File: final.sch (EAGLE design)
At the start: 84 parts, among them IC2 MEGA8-AI, IC4 7805, Q2 32.768kHz, U2 DS1307

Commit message: added holes and milling
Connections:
- removed net N$11: IC2.PB5(SCK), JP16.9
- removed net N$12: IC2.PB4(MISO), JP16.8
- removed net N$13: IC2.PB3(MOSI/OC2), JP16.7
- new net SELECT4.1: JP4.4, R36.2
- net MISO: now also IC2.PB4(MISO), JP16.8
- net MOSI: now also IC2.PB3(MOSI/OC2), JP16.7
- net SCK: now also IC2.PB5(SCK), JP16.9; no longer JP4.4, R36.2
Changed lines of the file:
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@@
 <net name="SCK" class="0">
-<segment>
-<pinref part="R36" gate="G$1" pin="2"/>
-<label x="464.82" y="5.08" size="1.778" layer="95"/>
-<pinref part="JP4" gate="A" pin="4"/>
-<wire x1="568.96" y1="137.16" x2="480.06" y2="137.16" width="0.1524" layer="91"/>
-<wire x1="480.06" y1="137.16" x2="480.06" y2="5.08" width="0.1524" layer="91"/>
-<wire x1="480.06" y1="5.08" x2="459.74" y2="5.08" width="0.1524" layer="91"/>
-<label x="546.1" y="137.16" size="1.778" layer="95"/>
-</segment>
 <segment>
 <pinref part="JP13" gate="A" pin="3"/>
 <wire x1="259.08" y1="-259.08" x2="248.92" y2="-259.08" width="0.1524" layer="91"/>
 <label x="248.92" y="-259.08" size="1.778" layer="95"/>
+</segment>
+<segment>
+<pinref part="IC2" gate="G$1" pin="PB5(SCK)"/>
+<label x="292.1" y="-223.52" size="1.778" layer="95"/>
+<pinref part="JP16" gate="A" pin="9"/>
+<wire x1="292.1" y1="-223.52" x2="330.2" y2="-223.52" width="0.1524" layer="91"/>
 </segment>
 </net>
@@
 <label x="248.92" y="-256.54" size="1.778" layer="95"/>
 </segment>
+<segment>
+<pinref part="IC2" gate="G$1" pin="PB4(MISO)"/>
+<wire x1="299.72" y1="-220.98" x2="297.18" y2="-220.98" width="0.1524" layer="91"/>
+<label x="292.1" y="-220.98" size="1.778" layer="95"/>
+<pinref part="JP16" gate="A" pin="8"/>
+<wire x1="297.18" y1="-220.98" x2="292.1" y2="-220.98" width="0.1524" layer="91"/>
+<wire x1="330.2" y1="-220.98" x2="299.72" y2="-220.98" width="0.1524" layer="91"/>
+</segment>
 </net>
 <net name="MOSI" class="0">
@@
 <wire x1="266.7" y1="-259.08" x2="276.86" y2="-259.08" width="0.1524" layer="91"/>
 <label x="271.78" y="-259.08" size="1.778" layer="95"/>
+</segment>
+<segment>
+<pinref part="IC2" gate="G$1" pin="PB3(MOSI/OC2)"/>
+<label x="292.1" y="-218.44" size="1.778" layer="95"/>
+<pinref part="JP16" gate="A" pin="7"/>
+<wire x1="330.2" y1="-218.44" x2="292.1" y2="-218.44" width="0.1524" layer="91"/>
 </segment>
 </net>
@@
 </segment>
 </net>
-<net name="N$11" class="0">
-<segment>
-<pinref part="IC2" gate="G$1" pin="PB5(SCK)"/>
-<label x="292.1" y="-223.52" size="1.778" layer="95"/>
-<pinref part="JP16" gate="A" pin="9"/>
-<wire x1="292.1" y1="-223.52" x2="330.2" y2="-223.52" width="0.1524" layer="91"/>
-</segment>
-</net>
-<net name="N$12" class="0">
-<segment>
-<pinref part="IC2" gate="G$1" pin="PB4(MISO)"/>
-<wire x1="299.72" y1="-220.98" x2="297.18" y2="-220.98" width="0.1524" layer="91"/>
-<label x="292.1" y="-220.98" size="1.778" layer="95"/>
-<pinref part="JP16" gate="A" pin="8"/>
-<wire x1="297.18" y1="-220.98" x2="292.1" y2="-220.98" width="0.1524" layer="91"/>
-<wire x1="330.2" y1="-220.98" x2="299.72" y2="-220.98" width="0.1524" layer="91"/>
-</segment>
-</net>
-<net name="N$13" class="0">
-<segment>
-<pinref part="IC2" gate="G$1" pin="PB3(MOSI/OC2)"/>
-<label x="292.1" y="-218.44" size="1.778" layer="95"/>
-<pinref part="JP16" gate="A" pin="7"/>
-<wire x1="330.2" y1="-218.44" x2="292.1" y2="-218.44" width="0.1524" layer="91"/>
-</segment>
-</net>
 <net name="N$15" class="0">
 <segment>
@@
 </segment>
 </net>
+<net name="SELECT4.1" class="0">
+<segment>
+<pinref part="R36" gate="G$1" pin="2"/>
+<label x="464.82" y="5.08" size="1.778" layer="95"/>
+<pinref part="JP4" gate="A" pin="4"/>
+<wire x1="568.96" y1="137.16" x2="480.06" y2="137.16" width="0.1524" layer="91"/>
+<wire x1="480.06" y1="137.16" x2="480.06" y2="5.08" width="0.1524" layer="91"/>
+<wire x1="480.06" y1="5.08" x2="459.74" y2="5.08" width="0.1524" layer="91"/>
+<label x="546.1" y="137.16" size="1.778" layer="95"/>
+</segment>
+</net>

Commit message: moved 1k resisitors on logic board, more compact. fixed inductor, diode and 7805 packages. TODO add ground plane, move holes, add milling
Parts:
- removed IC4: 7805, v-reg:LD117ADT18TR
- removed R10, R12, R14, R16, R18, R20, R73, R8, R9: 1k, eagle-ltspice:RR1206
- added IC1: LD117ADT12TR, v-reg:LD117ADT12TR
- added R24, R25, R26, R28, R30, R32, R33, R34, R35: 1k, eagle-ltspice:RR1206
- C13: value (none) -> 120pF
- C14, C15: value (none) -> 22uF
- C16: value 10uF -> 22uF
- C18: value 22uF -> 10uF
- R69: value (none) -> 13k
- R70: value (none) -> 200k
- R71, R72: value 1k -> 10k
- U$7: value INDUCTOR -> 15uH
- renumbered U$16 to U$6, U$17 to U$7, U$19 to U$8, U$20 to U$5
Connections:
- removed net N$1: JP3.1, R73.2
- new net N$48: JP16.1, R24.1
- net +5V: now also IC1.OUT; no longer IC4.OUT
- net GND: now also IC1.ADJ; no longer IC4.ADJ
- net MISO: now also R34.2; no longer JP16.8
- net MOSI: now also R32.2; no longer JP16.7
- net N$15: now also R33.2; no longer JP16.6
- net N$17: now also R30.2; no longer JP16.5
- net N$19: now also R28.2; no longer JP16.4
- net N$2: now also T17.B; no longer R8.2
- net N$21: now also R26.2; no longer JP16.3
- net N$26: now also JP3.1; no longer R73.1
- net N$27: now also JP16.3, R26.1; no longer R8.1, T17.B
- net N$28: now also JP3.3; no longer R9.1
- net N$29: now also JP3.4; no longer R10.1
- net N$3: now also JP16.9, R35.1; no longer JP3.3, R9.2
- net N$30: now also JP16.2, R25.1; no longer R12.1, T21.B
- net N$31: now also JP3.6; no longer R16.1
- net N$32: now also JP3.7; no longer R14.1
- net N$33: now also JP3.8; no longer R18.1
- net N$34: now also JP3.9; no longer R20.1
- net N$35: now also R25.2; no longer JP16.2
- net N$36: now also R24.2; no longer JP16.1
- net N$4: now also JP16.8, R34.1; no longer JP3.4, R10.2
- net N$5: now also T21.B; no longer R12.2
- net N$6: now also JP16.7, R32.1; no longer JP3.6, R16.2
- net N$7: now also JP16.6, R33.1; no longer JP3.7, R14.2
- net N$8: now also JP16.5, R30.1; no longer JP3.8, R18.2
- net N$9: now also JP16.4, R28.1; no longer JP3.9, R20.2
- net SCK: now also R35.2; no longer JP16.9
- net VCC: now also IC1.IN; no longer IC4.IN
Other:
- moved on the sheet: JP16

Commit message: shrinkified driver board. not OK
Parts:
- removed R19, R22, R23, R29, R36: 1k, eagle-ltspice:RR1206
- added R10, R12, R14, R8, R9: 1k, eagle-ltspice:RR1206
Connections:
- net 1.5V renamed 1.5VD
- removed net N$16: R19.1, T25.B
- removed net N$20: R23.1, T26.B
- removed net N$23: R29.1, T27.B
- removed net N$25: R36.1, T28.B
- removed net N$39: JP4.8, R22.1
- removed net SELECT4.1: JP4.4, R36.2
- new net 20VD: JP4.5, R1.2, R11.2, R13.2, R15.2, R17.2, R2.2, R21.2, R27.2, R3.2, R31.2, R4.2, R5.2, R6.2, R7.2
- new net N$11: JP17.1, R8.2
- new net N$12: JP17.2, R9.2
- new net N$13: JP17.3, R10.2
- new net N$40: JP17.4, R12.2
- new net N$41: JP17.8, R14.2
- new net SELECT1D: JP4.1, T25.B
- new net SELECT2D: JP4.2, T26.B
- new net SELECT3D: JP4.3, T27.B
- new net SELECT4.1D: JP4.4, T28.B
- net 20V: no longer JP4.5, R1.2, R11.2, R13.2, R15.2, R17.2, R2.2, R21.2, R27.2, R3.2, R31.2, R4.2, R5.2, R6.2, R7.2
- net N$37: now also R14.1; no longer JP17.8
- net N$38: now also JP4.8; no longer R22.2
- net SELECT1: now also R8.1; no longer JP17.1, JP4.1, R19.2
- net SELECT2: now also R10.1; no longer JP17.3, JP4.2, R23.2
- net SELECT3: now also R9.1; no longer JP17.2, JP4.3, R29.2
- net SELECT4: now also R12.1; no longer JP17.4

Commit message: driver board update, all components on bottom. still to large
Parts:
- removed R12: 1k, eagle-ltspice:RR1206
- added R16: 1k, eagle-ltspice:RR1206
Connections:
- removed net N$31: JP3.6, T24.B
- removed net N$32: JP3.7, T19.B
- removed net N$40: JP17.4, R12.2
- new net N$16: JP4.4, R10.2
- new net N$20: JP3.7, T24.B
- new net N$23: JP3.6, T19.B
- net N$11: now also JP4.1, R16.2; no longer JP17.1, R8.2
- net N$12: now also JP4.2, R8.2; no longer JP17.2, R9.2
- net N$13: now also JP4.3, R9.2; no longer JP17.3, R10.2
- net SEGMENT-D: now also R3.1, T17.C; no longer R4.1, T18.C
- net SEGMENT-E: now also R4.1, T18.C; no longer R3.1, T17.C
- net SELECT1: now also JP17.1; no longer R8.1
- net SELECT1D: now also R16.1; no longer JP4.1
- net SELECT2: now also JP17.3; no longer R10.1
- net SELECT2D: now also R8.1; no longer JP4.2
- net SELECT3: now also JP17.2; no longer R9.1
- net SELECT3D: now also R9.1; no longer JP4.3
- net SELECT4: now also JP17.4; no longer R12.1
- net SELECT4.1D: now also R10.1; no longer JP4.4
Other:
- moved on the sheet: R10, R8, R9

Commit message: thicker traces for switching supplies. milling almost done
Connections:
- removed net 1.5VD: JP4.6, U$1.FILAMENT1, U$2.FILAMENT1, U$3.FILAMENT1, U$4.FILAMENT1
- removed net N$11: JP4.1, R16.2
- removed net N$12: JP4.2, R8.2
- removed net N$13: JP4.3, R9.2
- removed net N$16: JP4.4, R10.2
- removed net N$2: JP3.2, T17.B
- removed net N$20: JP3.7, T24.B
- removed net N$23: JP3.6, T19.B
- removed net N$26: JP3.1, T15.B
- removed net N$27: JP16.3, R26.1
- removed net N$28: JP3.3, T18.B
- removed net N$29: JP3.4, T16.B
- removed net N$3: JP16.9, R35.1
- removed net N$30: JP16.2, R25.1
- removed net N$33: JP3.8, T20.B
- removed net N$34: JP3.9, T23.B
- removed net N$38: JP4.8, T22.B
- removed net N$4: JP16.8, R34.1
- removed net N$41: JP17.8, R14.2
- removed net N$48: JP16.1, R24.1
- removed net N$5: JP3.5, T21.B
- removed net N$6: JP16.7, R32.1
- removed net N$7: JP16.6, R33.1
- removed net N$8: JP16.5, R30.1
- removed net N$9: JP16.4, R28.1
- new net SEG1: JP17.8, JP4.8, R14.2, T22.B
- new net SEG10: JP16.9, JP3.9, R35.1, T23.B
- new net SEG2: JP16.1, JP3.1, R24.1, T15.B
- new net SEG3: JP16.2, JP3.2, R25.1, T17.B
- new net SEG4: JP16.3, JP3.3, R26.1, T18.B
- new net SEG5: JP16.4, JP3.4, R28.1, T16.B
- new net SEG6: JP16.5, JP3.5, R30.1, T21.B
- new net SEG7: JP16.6, JP3.6, R33.1, T19.B
- new net SEG8: JP16.7, JP3.7, R32.1, T24.B
- new net SEG9: JP16.8, JP3.8, R34.1, T20.B
- net 1V5: now also JP4.6, U$1.FILAMENT1, U$2.FILAMENT1, U$3.FILAMENT1, U$4.FILAMENT1
- net 20V: now also JP4.5, R31.2
- net 20VD: no longer JP4.5, R31.2
- net SELECT1: now also JP4.1, R16.2
- net SELECT2: now also JP4.3, R9.2
- net SELECT3: now also JP4.2, R8.2
- net SELECT4: now also JP4.4, R10.2
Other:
- moved on the sheet: R14

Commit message: fixed mirrored vfd layout
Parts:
- R71: value 10k -> 100k
- R72: value 10k -> 62k
- U$1, U$2, U$3, U$4: value VFD -> (none)
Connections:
- removed net 20VD: R1.2, R11.2, R13.2, R15.2, R17.2, R2.2, R21.2, R27.2, R3.2, R4.2, R5.2, R6.2, R7.2
- net 20V: now also R1.2, R11.2, R13.2, R15.2, R17.2, R2.2, R21.2, R27.2, R3.2, R4.2, R5.2, R6.2, R7.2
- net SEGMENT-A: now also R5.1, T19.C; no longer R15.1, T24.C
- net SEGMENT-B: now also R2.1, T16.C; no longer R13.1, T23.C
- net SEGMENT-C: now also R4.1, T18.C; no longer R11.1, T22.C
- net SEGMENT-DP: now also R7.1, T21.C; no longer R6.1, T20.C
- net SEGMENT-E: now also R11.1, T22.C; no longer R4.1, T18.C
- net SEGMENT-F: now also R13.1, T23.C; no longer R2.1, T16.C
- net SEGMENT-H: now also R15.1, T24.C; no longer R5.1, T19.C
- net SEGMENT-Q: now also R6.1, T20.C; no longer R7.1, T21.C

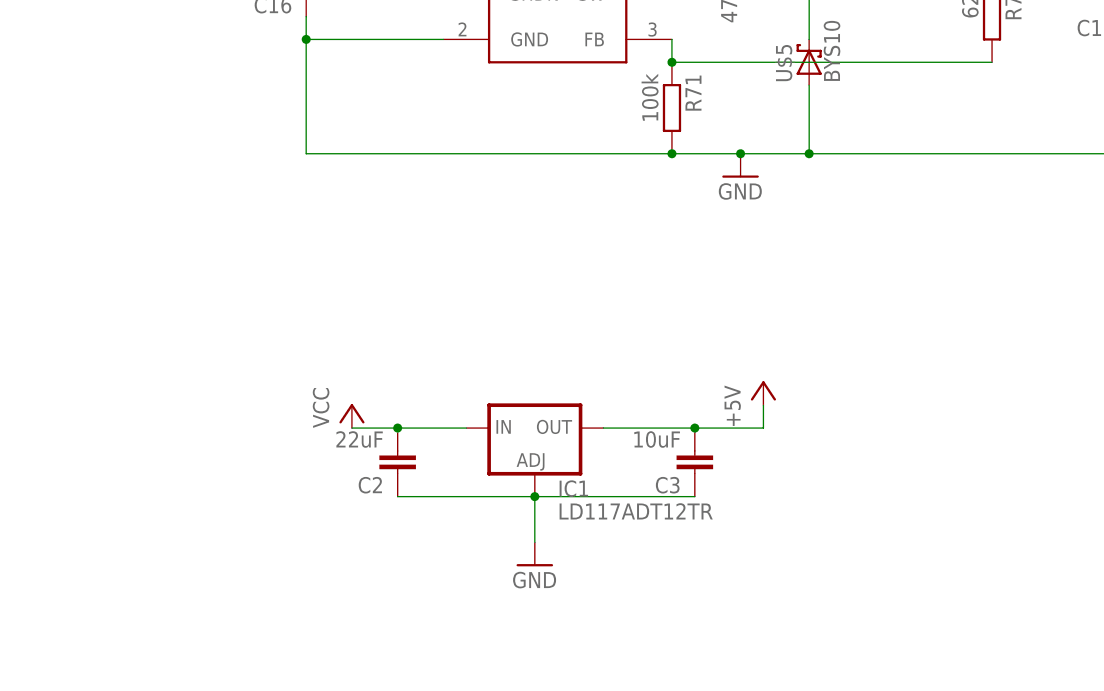
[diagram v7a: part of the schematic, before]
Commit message: added groundplane, replaced 5v regulator, added extra capacitors and optional diode / 0kresistor
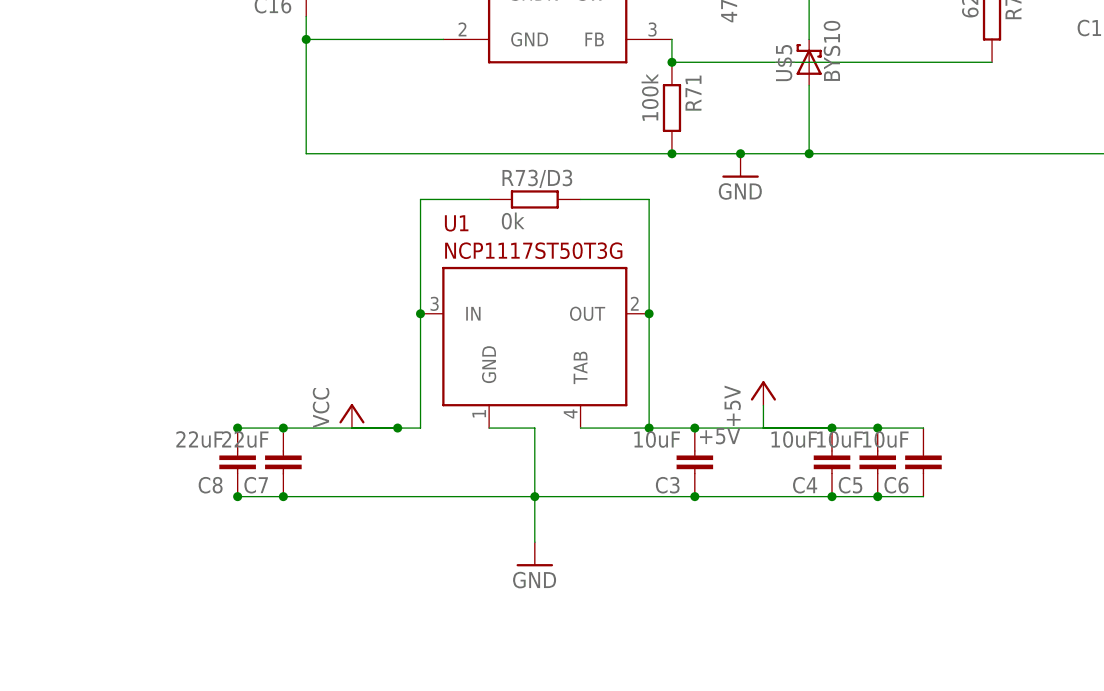
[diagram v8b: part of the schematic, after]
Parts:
- removed C2: 22uF, eagle-ltspice:CC1206
- removed IC1: LD117ADT12TR, v-reg:LD117ADT12TR
- added C4, C5, C6: 10uF, eagle-ltspice:CC1206
- added C7, C8: 22uF, eagle-ltspice:CC1206
- added R73/D3: 0k, eagle-ltspice:RR1206
- added U1: NCP1117ST50T3G, NCP1117ST50T3G:NCP1117ST50T3G
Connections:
- net +5V: now also C4.2, C5.2, C6.2, R73/D3.2, U1.OUT, U1.TAB; no longer IC1.OUT
- net GND: now also C4.1, C5.1, C6.1, C7.1, C8.1, U1.GND; no longer C2.1, IC1.ADJ
- net VCC: now also C7.2, C8.2, R73/D3.1, U1.IN; no longer C2.2, IC1.IN
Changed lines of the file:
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@@
 <part name="GND37" library="supply1" library_urn="urn:adsk.eagle:library:371" deviceset="GND" device=""/>
 <part name="C1" library="eagle-ltspice" library_urn="urn:adsk.eagle:library:217" deviceset="C" device="C1206" value="0.1uF"/>
-<part name="C2" library="eagle-ltspice" library_urn="urn:adsk.eagle:library:217" deviceset="C" device="C1206" value="22uF"/>
 <part name="C3" library="eagle-ltspice" library_urn="urn:adsk.eagle:library:217" deviceset="C" device="C1206" value="10uF"/>
 <part name="JP14" library="pinhead-2" deviceset="PINHD-1X02" device="_2.54"/>
@@
 <part name="U$7" library="djnr5020" deviceset="INDUCTOR" device="" value="15uH"/>
 <part name="U$8" library="djnr5020" deviceset="INDUCTOR" device="" value="15uH"/>
-<part name="IC1" library="v-reg" deviceset="LD117A?*" device="DT" technology="12TR"/>
 <part name="R14" library="eagle-ltspice" library_urn="urn:adsk.eagle:library:217" deviceset="R" device="R1206" value="1k"/>
 <part name="R16" library="eagle-ltspice" library_urn="urn:adsk.eagle:library:217" deviceset="R" device="R1206" value="1k"/>
@@
 <part name="U$3" library="VFD" deviceset="VFD" device=""/>
 <part name="U$4" library="VFD" deviceset="VFD" device=""/>
+<part name="U1" library="NCP1117ST50T3G" deviceset="NCP1117ST50T3G" device=""/>
+<part name="C4" library="eagle-ltspice" library_urn="urn:adsk.eagle:library:217" deviceset="C" device="C1206" value="10uF"/>
+<part name="C5" library="eagle-ltspice" library_urn="urn:adsk.eagle:library:217" deviceset="C" device="C1206" value="10uF"/>
+<part name="C6" library="eagle-ltspice" library_urn="urn:adsk.eagle:library:217" deviceset="C" device="C1206" value="10uF"/>
+<part name="C7" library="eagle-ltspice" library_urn="urn:adsk.eagle:library:217" deviceset="C" device="C1206" value="22uF"/>
+<part name="C8" library="eagle-ltspice" library_urn="urn:adsk.eagle:library:217" deviceset="C" device="C1206" value="22uF"/>
+<part name="R73/D3" library="eagle-ltspice" library_urn="urn:adsk.eagle:library:217" deviceset="R" device="R1206" value="0k"/>
 </parts>
 <sheets>
@@
 <instance part="GND37" gate="1" x="452.12" y="-276.86"/>
 <instance part="C1" gate="G$1" x="231.14" y="-200.66" rot="R180"/>
-<instance part="C2" gate="G$1" x="436.88" y="-266.7" rot="R180"/>
 <instance part="C3" gate="G$1" x="469.9" y="-266.7" rot="R180"/>
 <instance part="JP14" gate="A" x="279.4" y="-287.02"/>
@@
 <instance part="U$7" gate="G$1" x="454.66" y="-144.78" rot="R90"/>
 <instance part="U$8" gate="G$1" x="490.22" y="-208.28" rot="R90"/>
-<instance part="IC1" gate="G$1" x="452.12" y="-261.62"/>
 <instance part="R14" gate="G$1" x="332.74" y="-198.12" rot="MR180"/>
 <instance part="R16" gate="G$1" x="518.16" y="144.78" rot="MR180"/>
@@
 <instance part="U$3" gate="G$1" x="403.86" y="58.42"/>
 <instance part="U$4" gate="G$1" x="403.86" y="-2.54"/>
+<instance part="U1" gate="U1" x="452.12" y="-251.46"/>
+<instance part="C4" gate="G$1" x="485.14" y="-266.7" rot="R180"/>
+<instance part="C5" gate="G$1" x="490.22" y="-266.7" rot="R180"/>
+<instance part="C6" gate="G$1" x="495.3" y="-266.7" rot="R180"/>
+<instance part="C7" gate="G$1" x="424.18" y="-266.7" rot="R180"/>
+<instance part="C8" gate="G$1" x="419.1" y="-266.7" rot="R180"/>
+<instance part="R73/D3" gate="G$1" x="452.12" y="-236.22"/>
 </instances>
 <busses>
@@
 <pinref part="GND37" gate="1" pin="GND"/>
 <wire x1="452.12" y1="-269.24" x2="452.12" y2="-274.32" width="0.1524" layer="91"/>
-<pinref part="C2" gate="G$1" pin="1"/>
-<wire x1="436.88" y1="-269.24" x2="452.12" y2="-269.24" width="0.1524" layer="91"/>
+<wire x1="424.18" y1="-269.24" x2="452.12" y2="-269.24" width="0.1524" layer="91"/>
 <junction x="452.12" y="-269.24"/>
 <pinref part="C3" gate="G$1" pin="1"/>
 <wire x1="469.9" y1="-269.24" x2="452.12" y2="-269.24" width="0.1524" layer="91"/>
-<pinref part="IC1" gate="G$1" pin="ADJ"/>
+<pinref part="U1" gate="U1" pin="GND"/>
+<wire x1="447.04" y1="-261.62" x2="452.12" y2="-261.62" width="0.1524" layer="91"/>
+<wire x1="452.12" y1="-261.62" x2="452.12" y2="-269.24" width="0.1524" layer="91"/>
+<pinref part="C6" gate="G$1" pin="1"/>
+<wire x1="495.3" y1="-269.24" x2="490.22" y2="-269.24" width="0.1524" layer="91"/>
+<junction x="469.9" y="-269.24"/>
+<pinref part="C5" gate="G$1" pin="1"/>
+<wire x1="490.22" y1="-269.24" x2="485.14" y2="-269.24" width="0.1524" layer="91"/>
+<junction x="490.22" y="-269.24"/>
+<pinref part="C4" gate="G$1" pin="1"/>
+<wire x1="485.14" y1="-269.24" x2="469.9" y2="-269.24" width="0.1524" layer="91"/>
+<junction x="485.14" y="-269.24"/>
+<pinref part="C8" gate="G$1" pin="1"/>
+<pinref part="C7" gate="G$1" pin="1"/>
+<junction x="424.18" y="-269.24"/>
+<wire x1="424.18" y1="-269.24" x2="419.1" y2="-269.24" width="0.1524" layer="91"/>
+<junction x="419.1" y="-269.24"/>
 </segment>
 <segment>
@@
 <segment>
 <pinref part="P+20" gate="1" pin="+5V"/>
-<wire x1="459.74" y1="-261.62" x2="469.9" y2="-261.62" width="0.1524" layer="91"/>
-<wire x1="469.9" y1="-261.62" x2="477.52" y2="-261.62" width="0.1524" layer="91"/>
+<wire x1="469.9" y1="-261.62" x2="485.14" y2="-261.62" width="0.1524" layer="91"/>
+<wire x1="485.14" y1="-261.62" x2="477.52" y2="-261.62" width="0.1524" layer="91"/>
 <wire x1="477.52" y1="-261.62" x2="477.52" y2="-259.08" width="0.1524" layer="91"/>
 <pinref part="C3" gate="G$1" pin="2"/>
 <junction x="469.9" y="-261.62"/>
-<pinref part="IC1" gate="G$1" pin="OUT"/>
+<pinref part="U1" gate="U1" pin="OUT"/>
+<wire x1="469.9" y1="-261.62" x2="464.82" y2="-261.62" width="0.1524" layer="91"/>
+<wire x1="464.82" y1="-261.62" x2="464.82" y2="-248.92" width="0.1524" layer="91"/>
+<pinref part="U1" gate="U1" pin="TAB"/>
+<wire x1="457.2" y1="-261.62" x2="464.82" y2="-261.62" width="0.1524" layer="91"/>
+<junction x="464.82" y="-261.62"/>
+<pinref part="C4" gate="G$1" pin="2"/>
+<junction x="485.14" y="-261.62"/>
+<label x="474.98" y="-261.62" size="1.778" layer="95" rot="R180"/>
+<pinref part="C6" gate="G$1" pin="2"/>
+<wire x1="495.3" y1="-261.62" x2="490.22" y2="-261.62" width="0.1524" layer="91"/>
+<pinref part="C5" gate="G$1" pin="2"/>
+<wire x1="490.22" y1="-261.62" x2="485.14" y2="-261.62" width="0.1524" layer="91"/>
+<junction x="490.22" y="-261.62"/>
+<wire x1="464.82" y1="-248.92" x2="464.82" y2="-236.22" width="0.1524" layer="91"/>
+<junction x="464.82" y="-248.92"/>
+<pinref part="R73/D3" gate="G$1" pin="2"/>
+<wire x1="464.82" y1="-236.22" x2="457.2" y2="-236.22" width="0.1524" layer="91"/>
 </segment>
 <segment>
@@
 <pinref part="P+19" gate="VCC" pin="VCC"/>
 <wire x1="431.8" y1="-261.62" x2="436.88" y2="-261.62" width="0.1524" layer="91"/>
-<pinref part="C2" gate="G$1" pin="2"/>
-<wire x1="436.88" y1="-261.62" x2="444.5" y2="-261.62" width="0.1524" layer="91"/>
+<wire x1="436.88" y1="-261.62" x2="439.42" y2="-261.62" width="0.1524" layer="91"/>
 <junction x="436.88" y="-261.62"/>
-<pinref part="IC1" gate="G$1" pin="IN"/>
-</segment>
-<segment>
+<pinref part="U1" gate="U1" pin="IN"/>
+<wire x1="439.42" y1="-261.62" x2="439.42" y2="-248.92" width="0.1524" layer="91"/>
+<pinref part="C8" gate="G$1" pin="2"/>
+<wire x1="436.88" y1="-261.62" x2="424.18" y2="-261.62" width="0.1524" layer="91"/>
+<wire x1="424.18" y1="-261.62" x2="419.1" y2="-261.62" width="0.1524" layer="91"/>
+<wire x1="439.42" y1="-248.92" x2="439.42" y2="-236.22" width="0.1524" layer="91"/>
+<junction x="439.42" y="-248.92"/>
+<pinref part="R73/D3" gate="G$1" pin="1"/>
+<wire x1="439.42" y1="-236.22" x2="447.04" y2="-236.22" width="0.1524" layer="91"/>
+<junction x="419.1" y="-261.62"/>
+<pinref part="C7" gate="G$1" pin="2"/>
+<junction x="424.18" y="-261.62"/>
+</segment>
+<segment>
